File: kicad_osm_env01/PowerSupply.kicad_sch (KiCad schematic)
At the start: 30 parts, among them J4 Conn_01x02, J5 USB_C_Receptacle_USB2.0, U1 LM66100DCKR, U4 LM66100DCKR, U9 TLV1117LV33DCYR

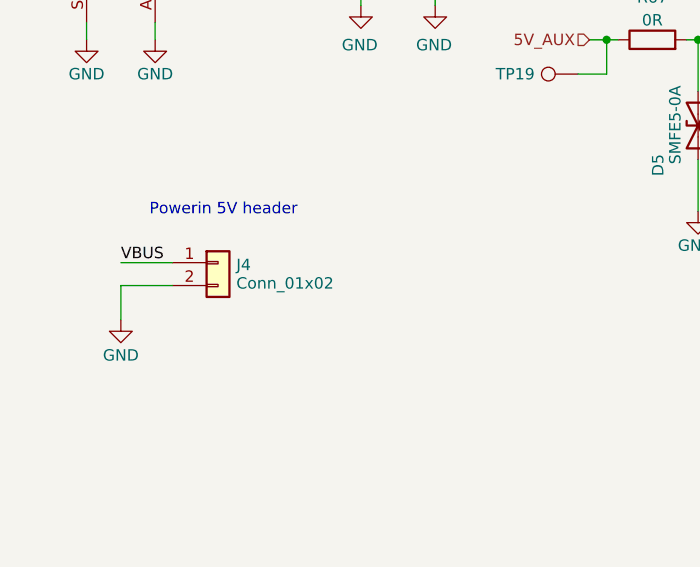
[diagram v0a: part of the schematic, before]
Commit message: added information to symbol entries table, added jumper settings table, minor single track update on layout
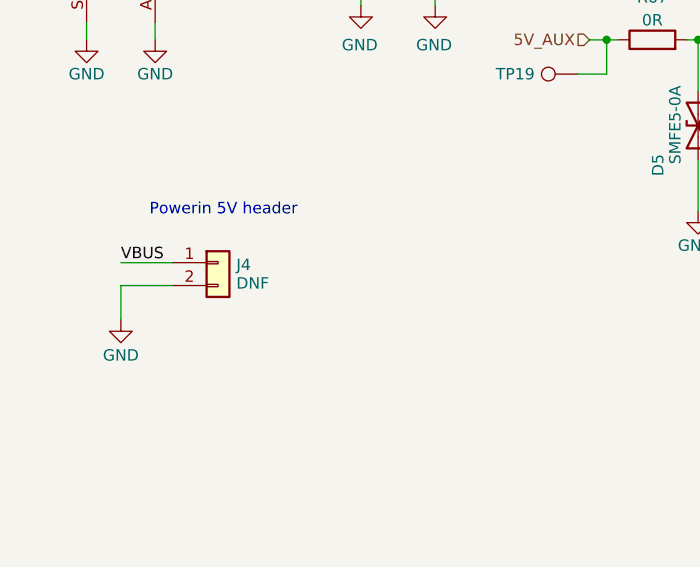
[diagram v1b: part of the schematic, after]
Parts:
- C10, C9: Characteristics (none) -> X5R; Voltage (none) -> 10V
- C26, C6: Characteristics (none) -> X5R; Other (none) -> Can use own part, but needs to meet the specs; Voltage (none) -> 10V
- C31, C7: Characteristics (none) -> X5R; Other (none) -> Can use own part, but needs to meet the specs
- D2, D5: Manufacturer (none) -> SMFE5-0A; Manufacturer Part Number (none) -> Eaton - Electronics Division
- J4: value Conn_01x02 -> DNF
- J5: Manufacturer (none) -> Molex; Manufacturer Part Number (none) -> 216989-0001
- R23, R320, R321, R45, R65, R66, R67, R68: Tolerance (none) -> 1%
- U1, U4: Manufacturer (none) -> Texas Instruments; Manufacturer Part Number (none) -> LM66100DCKR
- U9: Manufacturer (none) -> Texas Instruments; Manufacturer Part Number (none) -> TLV1117LV33DCYR

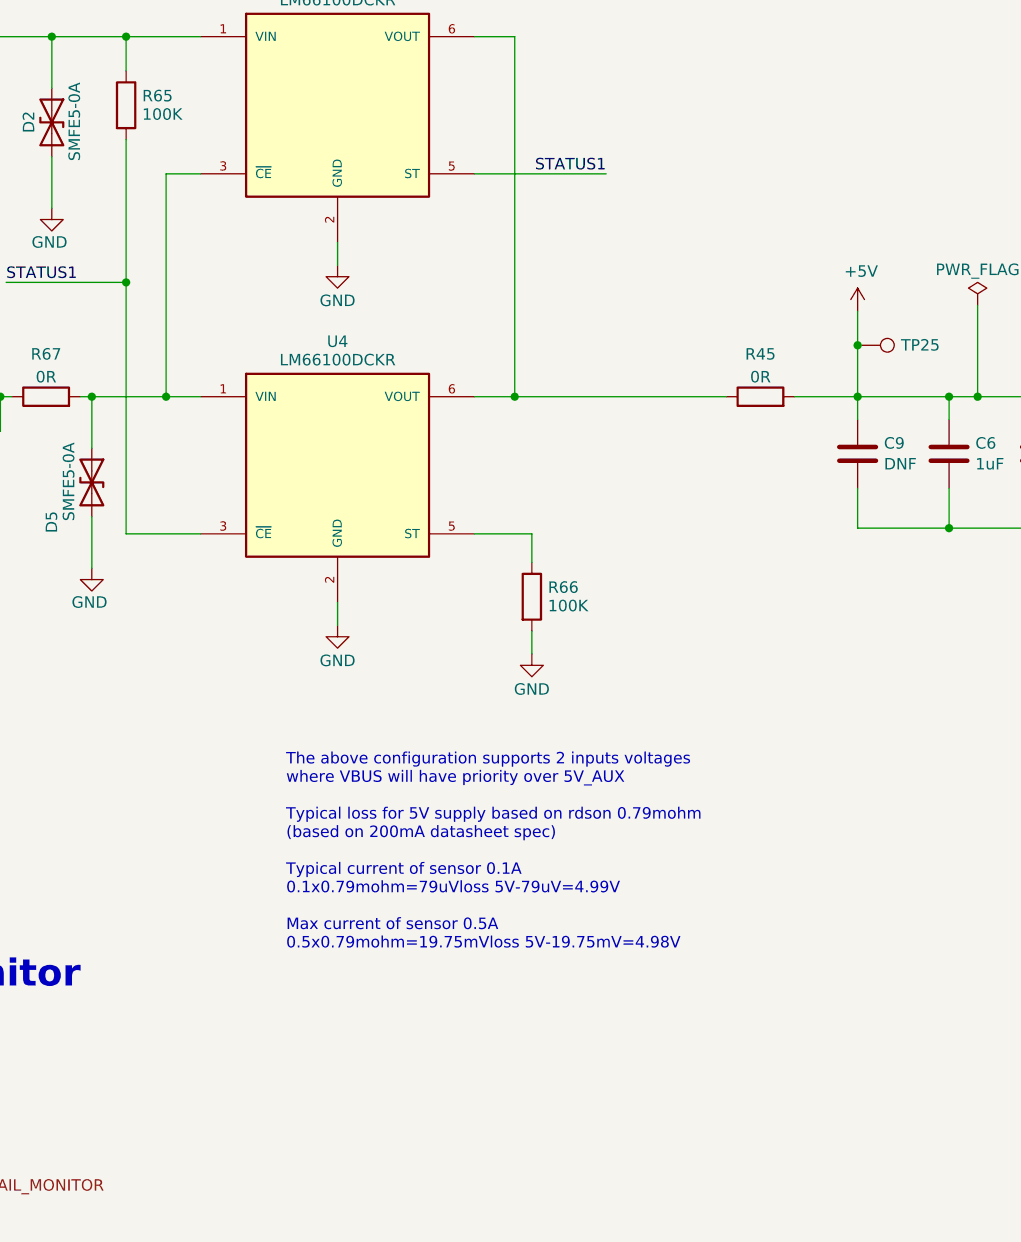
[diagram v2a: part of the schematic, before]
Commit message: schematic and layout changes based on first round of review comments
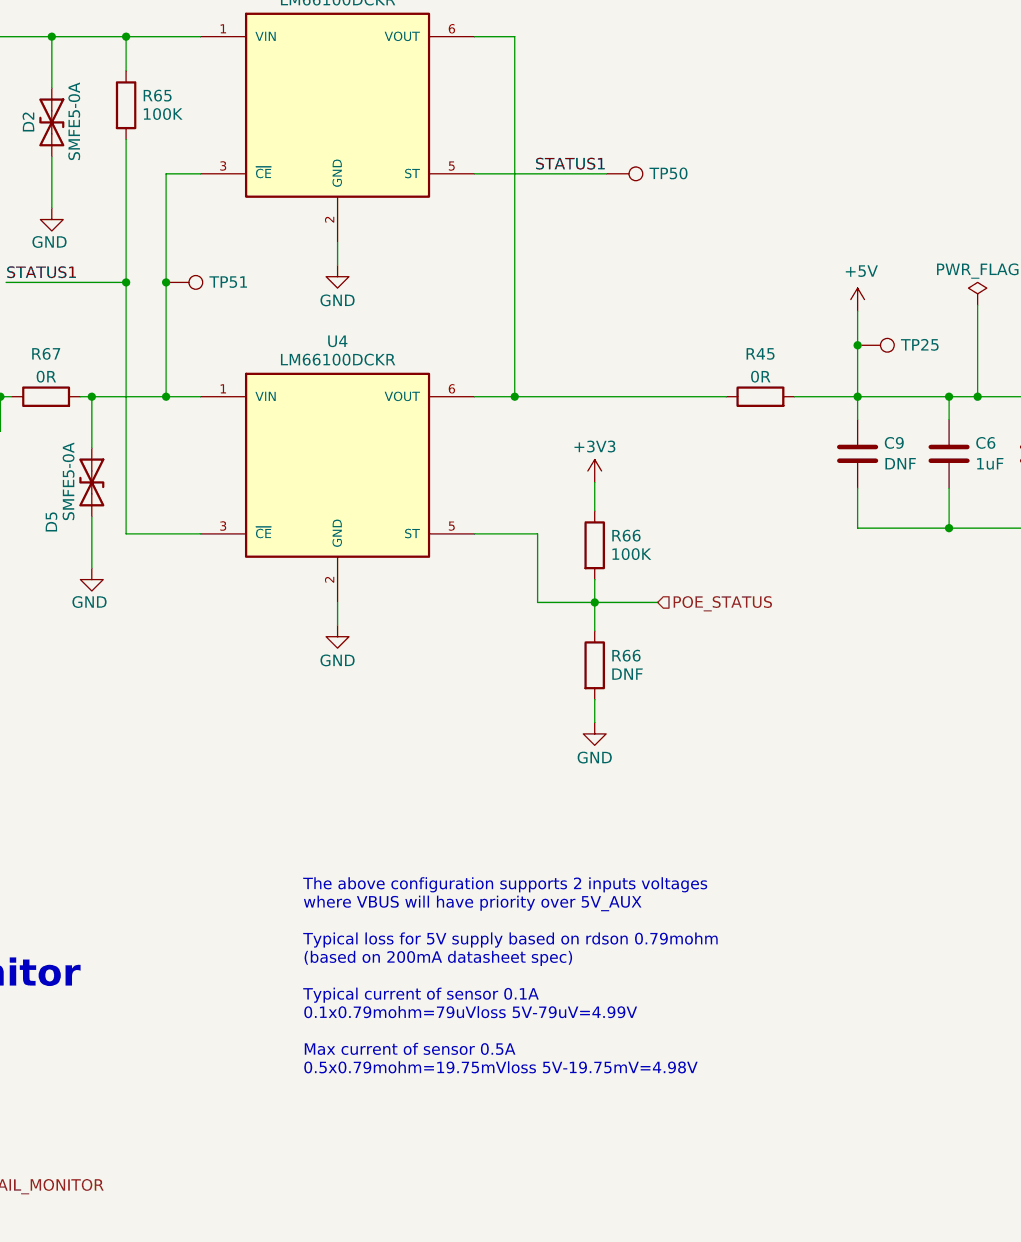
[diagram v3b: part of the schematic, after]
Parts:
- added R66: 100K, Resistor_SMD:R_0402_1005Metric, symbol Device:R
- added TP50, TP51: Test_Point, TestPoint:TestPoint_Pad_D1.5mm, symbol OSM_env01-rescue:Test_Point-Connector-ESP32-EVB_Rev_D-rescue
- R66: value 100K -> DNF
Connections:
- net +3V3: now also R66.1
- net STATUS1: now also TP50.1
- net at D5.1 (A1), R67.2, U1.3 (~{CE})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: now also TP51.1
- net POE_STATUS: now reaches R66.1, U4.5 (ST)
- net POE_STATUS: now also R66.2
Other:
- moved on the sheet: R66

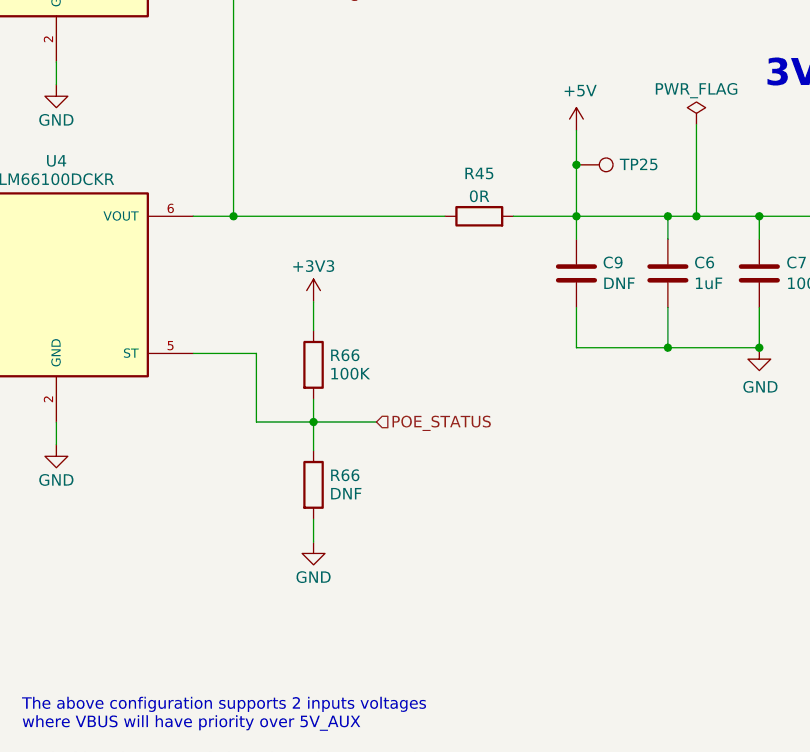
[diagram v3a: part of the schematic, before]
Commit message: removed 0R links and DNF parts on schematics
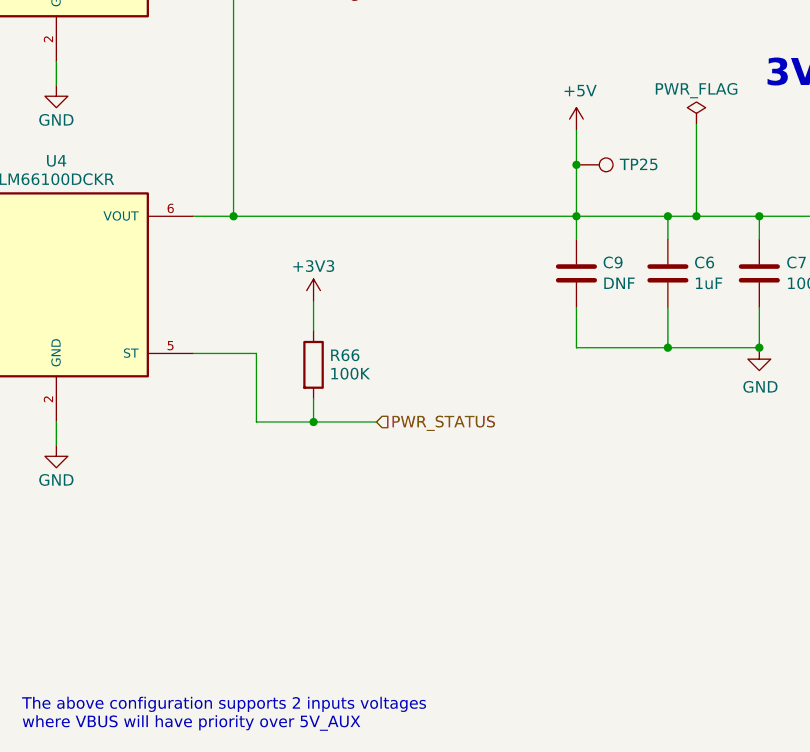
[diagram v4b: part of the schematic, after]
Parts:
- removed R45: 0R, Resistor_SMD:R_0805_2012Metric, symbol Device:R
- removed R66: DNF, Resistor_SMD:R_0402_1005Metric, symbol Device:R
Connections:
- net +5V: now also U1.6 (VOUT), U4.6 (VOUT)
- net POE_STATUS renamed PWR_STATUS
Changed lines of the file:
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@@
-    (stroke (width 0) (type default))
-  )
-  (wire (pts (xy 146.685 98.425) (xy 146.685 101.6))
     (stroke (width 0) (type default))
   )
@@
     (stroke (width 0) (type default))
   )
-  (wire (pts (xy 168.91 75.565) (xy 175.895 75.565))
-    (stroke (width 0) (type default))
-  )
   (wire (pts (xy 32.385 102.87) (xy 26.67 102.87))
     (stroke (width 0) (type default))
@@
     (stroke (width 0) (type default))
   )
-  (wire (pts (xy 137.795 75.565) (xy 161.29 75.565))
+  (wire (pts (xy 137.795 75.565) (xy 175.895 75.565))
     (stroke (width 0) (type default))
   )
@@
   )
   (wire (pts (xy 71.755 35.56) (xy 86.36 35.56))
-    (stroke (width 0) (type default))
-  )
-  (wire (pts (xy 146.685 109.22) (xy 146.685 111.76))
     (stroke (width 0) (type default))
   )
@@
     (effects (font (size 1.27 1.27)) (justify left bottom))
   )
-  (hierarchical_label "POE_STATUS" (shape input) (at 153.67 98.425 0) (fields_autoplaced)
+  (hierarchical_label "PWR_STATUS" (shape input) (at 153.67 98.425 0) (fields_autoplaced)
     (effects (font (size 1.27 1.27)) (justify left))
   )
@@
     )
   )
-  (symbol (lib_id "Device:R") (at 146.685 105.41 0) (unit 1)
-    (in_bom yes) (on_board yes) (dnp no) (fields_autoplaced)
-    (property "Reference" "R66" (at 148.463 104.386 0)
-      (effects (font (size 1.27 1.27)) (justify left))
-    )
-    (property "Value" "DNF" (at 148.463 106.434 0)
-      (effects (font (size 1.27 1.27)) (justify left))
-    )
-    (property "Footprint" "Resistor_SMD:R_0402_1005Metric" (at 144.907 105.41 90)
-      (effects (font (size 1.27 1.27)) hide)
-    )
-    (property "Datasheet" "" (at 146.685 105.41 0)
-      (effects (font (size 1.27 1.27)) hide)
-    )
-    (property "Tolerance" "1%" (at 146.685 105.41 0)
-      (effects (font (size 1.27 1.27)) hide)
-    )
-    (property "Power Rating" "" (at 146.685 105.41 0)
-      (effects (font (size 1.27 1.27)) hide)
-    )
-    (property "Current Rating" "" (at 146.685 105.41 0)
-      (effects (font (size 1.27 1.27)) hide)
-    )
-    (pin "1")
-    (pin "2")
-    (instances
-      (project "OSM_env01"
-        (path "/ab8b0540-9c9f-4195-88f5-7bed0b0a8ed6"
-          (reference "R66") (unit 1)
-        )
-        (path "/ab8b0540-9c9f-4195-88f5-7bed0b0a8ed6/00000000-0000-0000-0000-000060688d25"
-          (reference "R66") (unit 1)
-        )
-      )
-    )
-  )
   (symbol (lib_id "Device:C") (at 227.965 81.915 0) (mirror y) (unit 1)
     (in_bom yes) (on_board yes) (dnp no)
@@
         (path "/ab8b0540-9c9f-4195-88f5-7bed0b0a8ed6/00000000-0000-0000-0000-000060688d25"
           (reference "#PWR044") (unit 1)
-        )
-      )
-    )
-  )
-  (symbol (lib_id "OSM_env01:GND") (at 146.685 111.76 0) (unit 1)
-    (in_bom yes) (on_board yes) (dnp no) (fields_autoplaced)
-    (property "Reference" "#PWR088" (at 146.685 118.11 0)
-      (effects (font (size 1.27 1.27)) hide)
-    )
-    (property "Value" "GND" (at 146.685 115.705 0)
-      (effects (font (size 1.27 1.27)))
-    )
-    (property "Footprint" "" (at 146.685 111.76 0)
-      (effects (font (size 1.524 1.524)))
-    )
-    (property "Datasheet" "" (at 146.685 111.76 0)
-      (effects (font (size 1.524 1.524)))
-    )
-    (pin "1")
-    (instances
-      (project "OSM_env01"
-        (path "/ab8b0540-9c9f-4195-88f5-7bed0b0a8ed6"
-          (reference "#PWR088") (unit 1)
-        )
-        (path "/ab8b0540-9c9f-4195-88f5-7bed0b0a8ed6/00000000-0000-0000-0000-000060688d25"
-          (reference "#PWR091") (unit 1)
         )
       )
@@
         )
       )
-    )
-  )
-  (symbol (lib_id "Device:R") (at 165.1 75.565 90) (unit 1)
-    (in_bom yes) (on_board yes) (dnp no) (fields_autoplaced)
-    (property "Reference" "R45" (at 165.1 70.8492 90)
-      (effects (font (size 1.27 1.27)))
-    )
-    (property "Value" "0R" (at 165.1 73.3861 90)
-      (effects (font (size 1.27 1.27)))
-    )
-    (property "Footprint" "Resistor_SMD:R_0805_2012Metric" (at 165.1 77.343 90)
-      (effects (font (size 1.27 1.27)) hide)
-    )
-    (property "Datasheet" "" (at 165.1 75.565 0)
-      (effects (font (size 1.27 1.27)) hide)
-    )
-    (property "Tolerance" "1%" (at 165.1 75.565 0)
-      (effects (font (size 1.27 1.27)) hide)
-    )
-    (property "Power Rating" "" (at 165.1 75.565 0)
-      (effects (font (size 1.27 1.27)) hide)
-    )
-    (property "Current Rating" "" (at 165.1 75.565 0)
-      (effects (font (size 1.27 1.27)) hide)
-    )
-    (pin "1")
-    (pin "2")
-    (instances
-      (project "OSM_env01"
-        (path "/ab8b0540-9c9f-4195-88f5-7bed0b0a8ed6/00000000-0000-0000-0000-000060688d25"
-          (reference "R45") (unit 1)
-        )
-      )

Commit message: minor update to layout
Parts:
- removed R67: 0R, Resistor_SMD:R_0805_2012Metric, symbol Device:R
- removed TP51: Test_Point, TestPoint:TestPoint_Pad_D1.5mm, symbol OSM_env01-rescue:Test_Point-Connector-ESP32-EVB_Rev_D-rescue
- added D32: RB160M-40TR, Diode_SMD:D_SOD-123, symbol moto_board-rescue:D-device-Sensi_Board-rescue-Motor_Control_Board-rescue
- added TP1: Test_Point, Devtank_PCB_lib:TestPoint_Pad_D1.5mm, symbol OSM_env01-rescue:Test_Point-Connector-ESP32-EVB_Rev_D-rescue
- R112, R113, R18, R19, R320, R321, R65, R66: Other (none) -> Can use own part, but needs to meet the specs
- R23, R68: Current Rating (none) -> 2A; Other (none) -> Can use own part, but needs to meet the specs
- TP18, TP19, TP25, TP26, TP50, TP8: footprint TestPoint:TestPoint_Pad_D1.5mm -> Devtank_PCB_lib:TestPoint_Pad_D1.5mm
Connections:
- net +5V: now also D32.1 (K)
- net 5V_AUX: now also D5.1 (A1), U1.3 (~{CE}), U4.1 (VIN)
- net at C10.1, C26.1, C31.1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: now also D32.2 (A), TP1.1

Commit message: Rev D finished, minor update to bom, schematic exported and folder structure updated
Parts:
- C31, C7: Characteristics X5R -> C0G/NP0
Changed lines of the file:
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@@
   (title_block
     (title "Open Smart Monitor")
-    (date "2023-12-08")
+    (date "2023-12-19")
     (rev "D")
     (company "Devtank LTD")
@@
       (effects (font (size 1.27 1.27)) hide)
     )
-    (property "Characteristics" "X5R" (at 227.965 81.915 0)
+    (property "Characteristics" "C0G/NP0" (at 227.965 81.915 0)
       (effects (font (size 1.27 1.27)) hide)
     )
@@
       (effects (font (size 1.27 1.27)) hide)
     )
-    (property "Characteristics" "X5R" (at 196.215 81.915 0)
-      (effects (font (size 1.27 1.27)) hide)
-    )
+    (property "Characteristics" "C0G/NP0" (at 196.215 81.915 0)
+      (effects (font (size 1.27 1.27)) hide)
+    )
